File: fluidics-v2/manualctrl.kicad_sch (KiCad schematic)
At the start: 25 parts, among them SW1 D6C90F1LFS, U6 TCA9539PWR

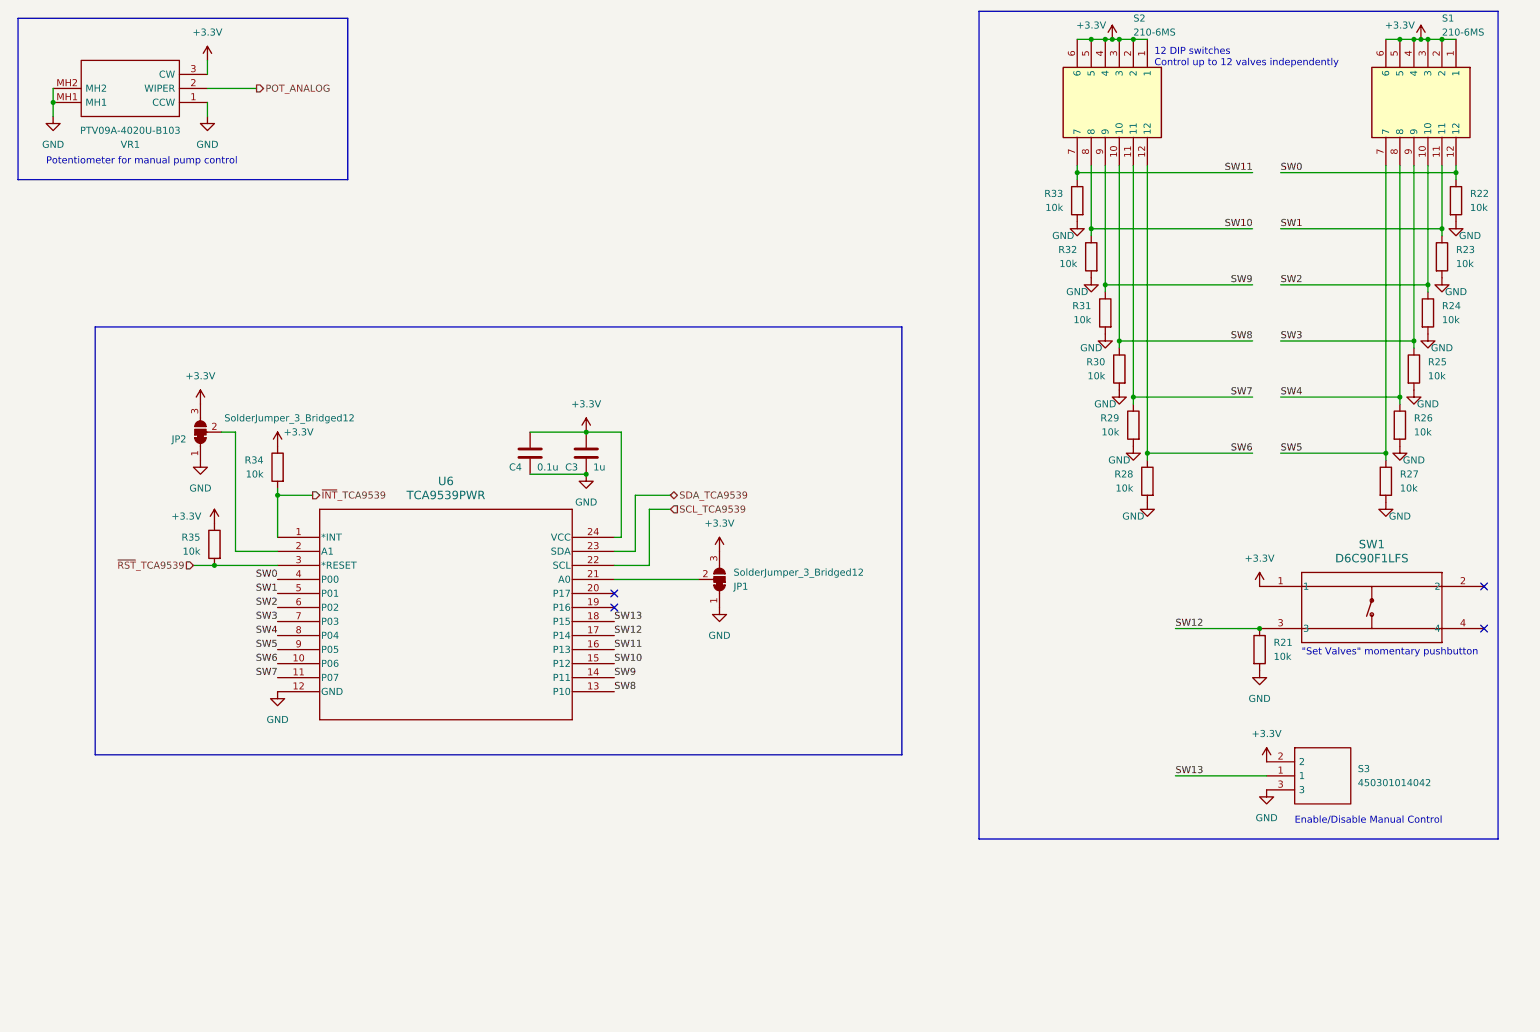
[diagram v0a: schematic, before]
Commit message: added footprints and mounting holes, cleaned up some sheets
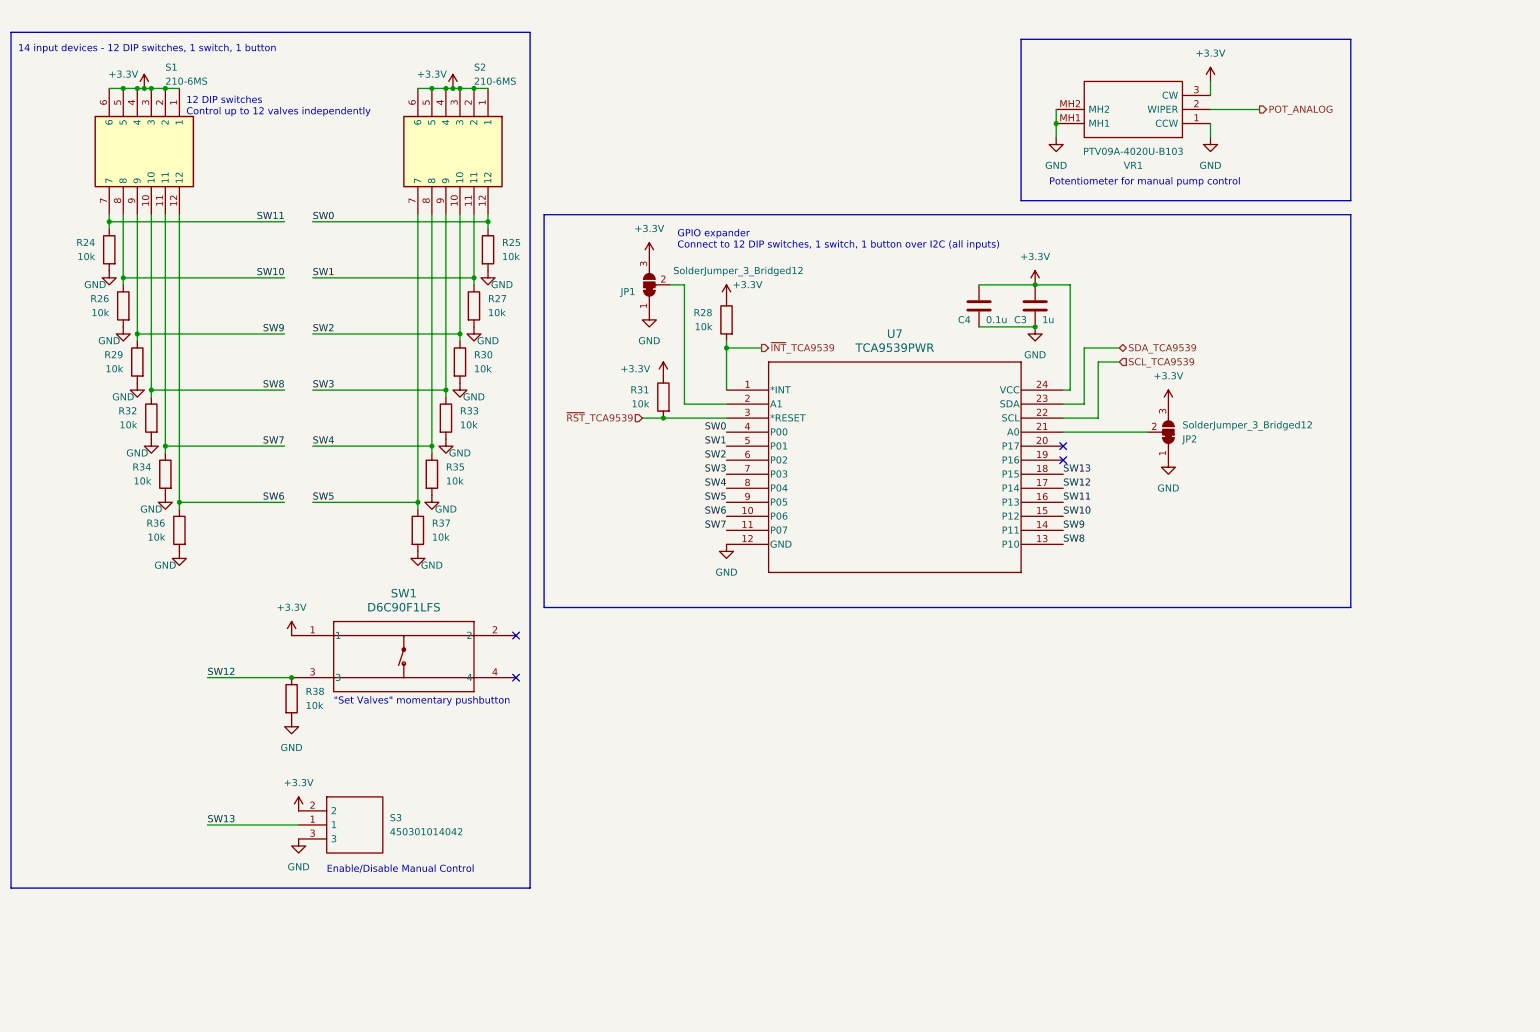
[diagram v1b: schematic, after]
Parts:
- renumbered JP2 to JP1, JP1 to JP2, R33 to R24, R22 to R25, R32 to R26, R23 to R27, R34 to R28, R31 to R29, R24 to R30, R35 to R31, R30 to R32, R25 to R33, R29 to R34, R26 to R35, R28 to R36, R27 to R37, R21 to R38, S2 to S1, S1 to S2, U6 to U7
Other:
- note added: "14 input devices - 12 DIP switches, 1 switch, 1 button"
- note added: "GPIO expander Connect to 12 DIP switches, 1 switch, 1 button over I2C (all inputs)"
- moved on the sheet: C3, C4, JP1, JP2, R24, R25, R26, R27, R28, R29, R30, R31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

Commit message: added missing footprint
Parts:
- JP1, JP2: footprint (none) -> Jumper:SolderJumper-3_P1.3mm_Bridged12_Pad1.0x1.5mm_NumberLabels
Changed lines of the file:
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@@
       (effects (font (size 1.27 1.27)) (justify left))
     )
-    (property "Footprint" "" (at 130.81 62.23 0)
+    (property "Footprint" "Jumper:SolderJumper-3_P1.3mm_Bridged12_Pad1.0x1.5mm_NumberLabels" (at 130.81 62.23 0)
       (effects (font (size 1.27 1.27)) hide)
     )
@@
       (effects (font (size 1.27 1.27)) (justify left))
     )
-    (property "Footprint" "" (at 224.79 88.9 0)
+    (property "Footprint" "Jumper:SolderJumper-3_P1.3mm_Bridged12_Pad1.0x1.5mm_NumberLabels" (at 224.79 88.9 0)
       (effects (font (size 1.27 1.27)) hide)
     )

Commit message: new version
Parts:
- added S4: 450301014042, wurth:450301014042, symbol 450301014042:450301014042
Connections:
- net +3.3V: now also S4.2
- net GND: now also S4.3
- net SW14: now reaches U7.19 (P16)
- net SW14: now also S4.1
- no-connect marks 4 -> 3
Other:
- note added: "Pressure/Vacuum selector (sets valves 1/4 to either be both on or both off)"

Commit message: started layout
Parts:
- renumbered C4 to C?, C3 to C?, R24 to R26, R26 to R27, R29 to R28, R32 to R29, R34 to R30, R36 to R31, R38 to R32, R37 to R33, R35 to R34, R33 to R35, R30 to R36, R27 to R37, R25 to R38, R31 to R39, R28 to R40, S3 to S2, S4 to S3, S2 to S4, U7 to U8

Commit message: added pressure controllers and more flow sensors
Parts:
- C?: footprint Capacitor_SMD:C_0603_1608Metric -> Capacitor_SMD:C_0805_2012Metric
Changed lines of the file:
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@@
       (effects (font (size 1.27 1.27)) (justify left))
     )
-    (property "Footprint" "Capacitor_SMD:C_0603_1608Metric" (at 201.6252 69.85 0)
+    (property "Footprint" "Capacitor_SMD:C_0805_2012Metric" (at 201.6252 69.85 0)
       (effects (font (size 1.27 1.27)) hide)
     )

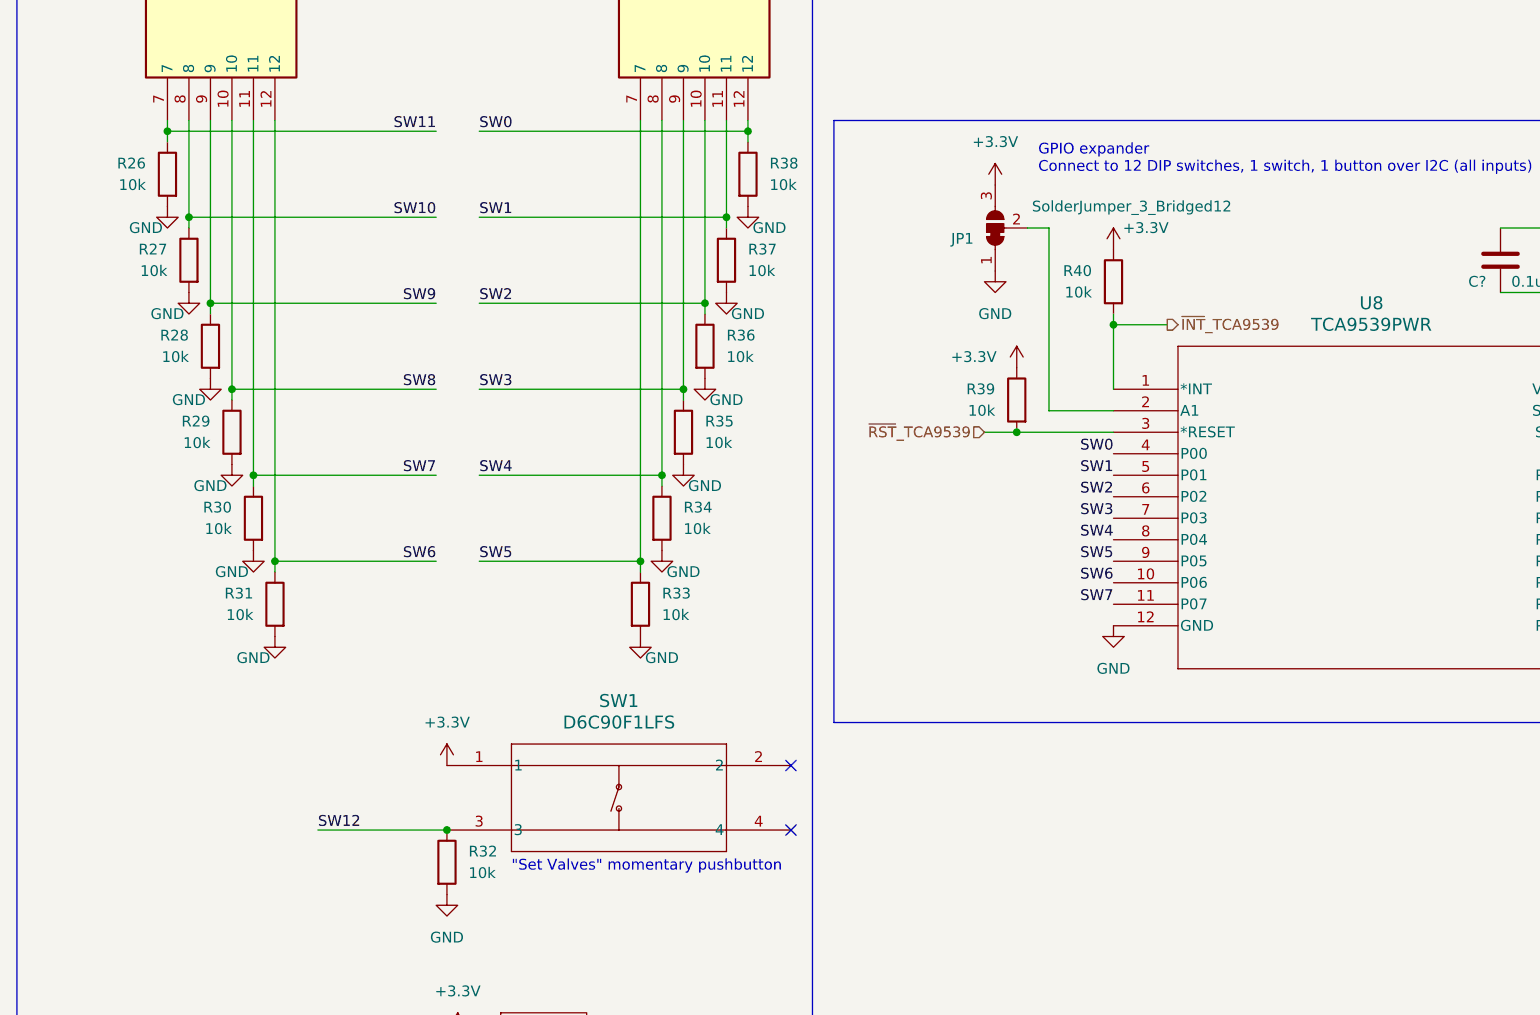
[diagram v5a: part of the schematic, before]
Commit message: added new connector for motor control daughter board. began layout
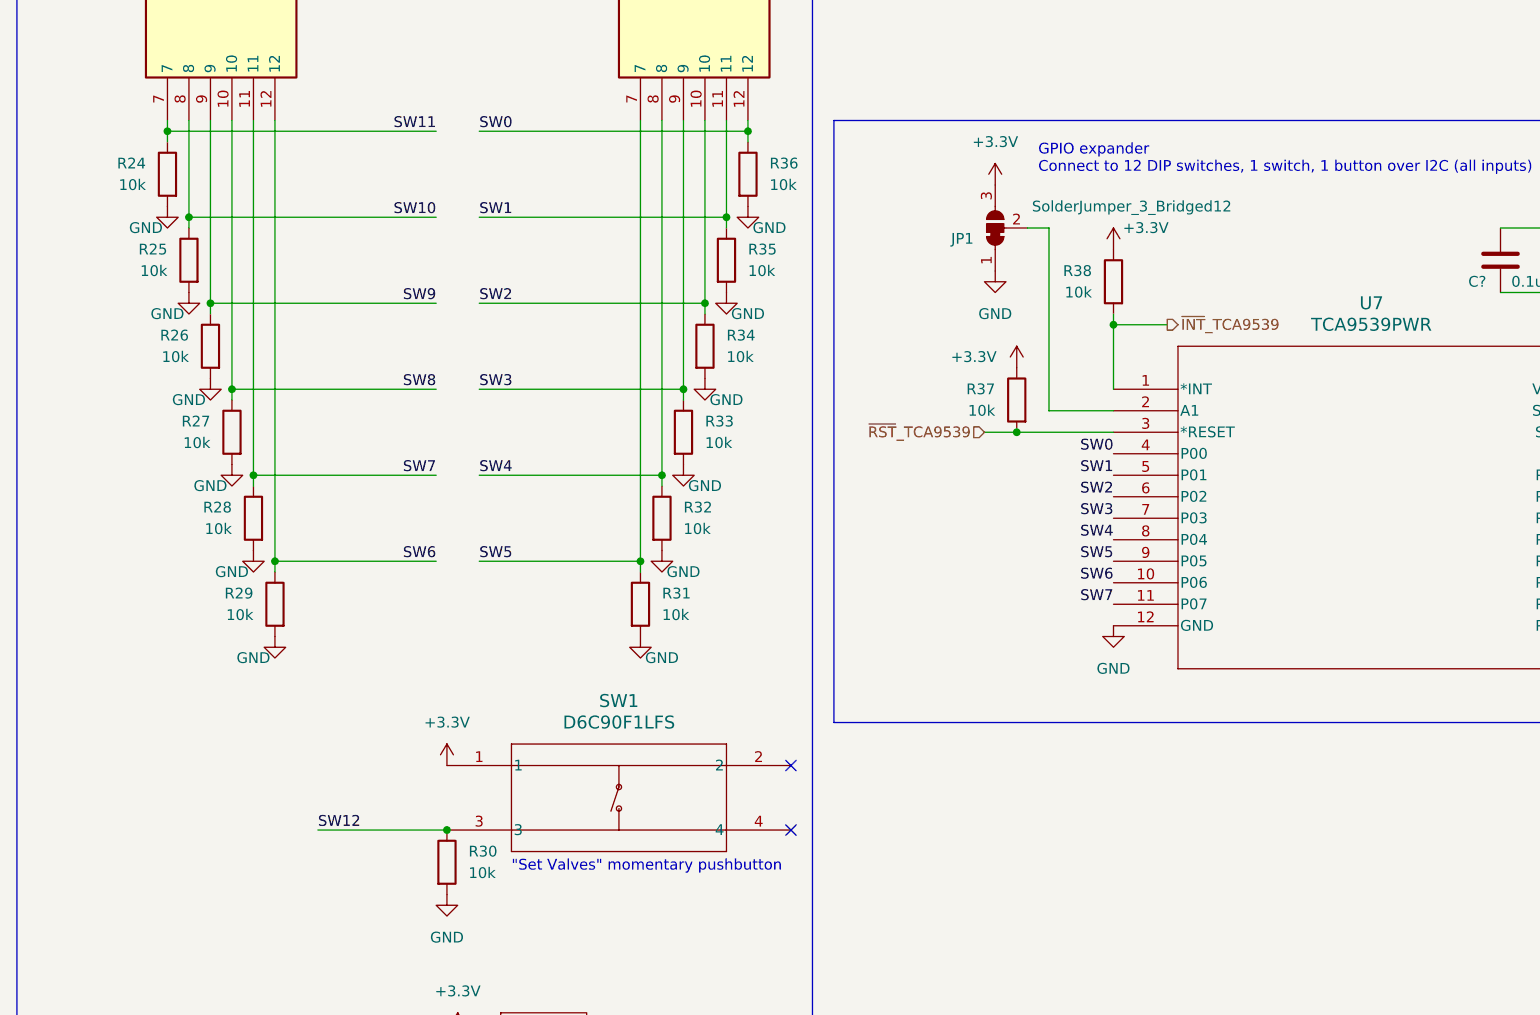
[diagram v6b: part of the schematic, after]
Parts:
- renumbered R26 to R24, R27 to R25, R28 to R26, R29 to R27, R30 to R28, R31 to R29, R32 to R30, R33 to R31, R34 to R32, R35 to R33, R36 to R34, R37 to R35, R38 to R36, R39 to R37, R40 to R38, U8 to U7

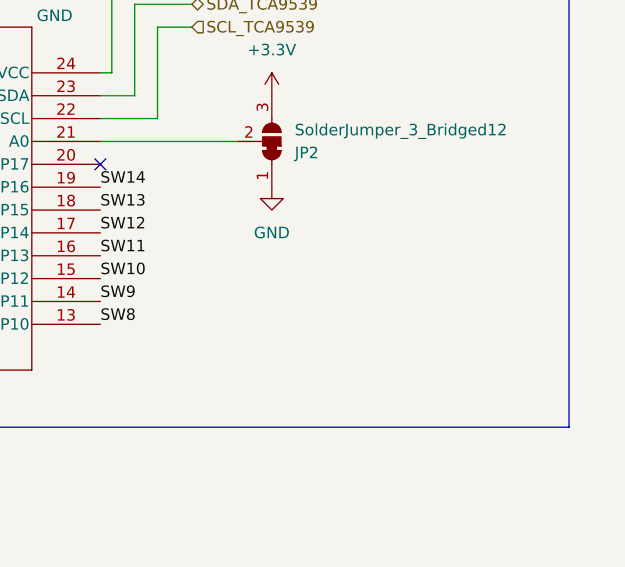
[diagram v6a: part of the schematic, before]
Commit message: added pullups/downs to spi for stability, rounded corners
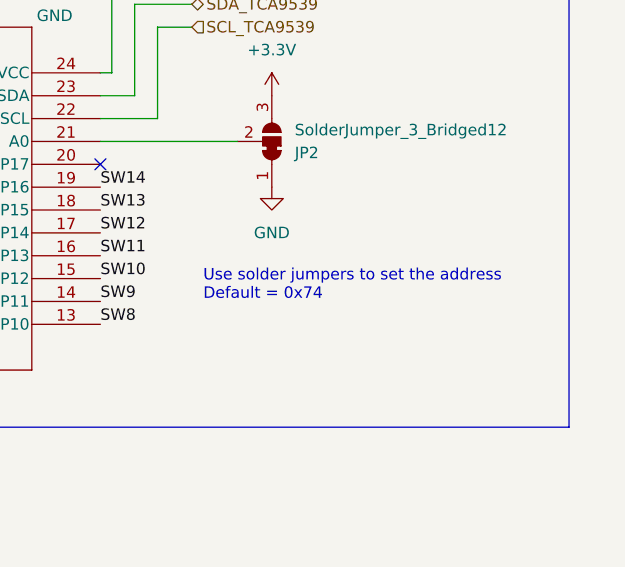
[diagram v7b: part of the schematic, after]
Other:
- note added: "Use solder jumpers to set the address Default = 0x74"
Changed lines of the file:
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@@
+    (effects (font (size 1.27 1.27)) (justify left bottom))
+  )
+  (text "Use solder jumpers to set the address\nDefault = 0x74"
+    (at 217.17 106.68 0)
     (effects (font (size 1.27 1.27)) (justify left bottom))
   )
